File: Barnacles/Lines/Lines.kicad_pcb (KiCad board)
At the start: 2 copper layers, 10 x 88.8 mm, 6 parts

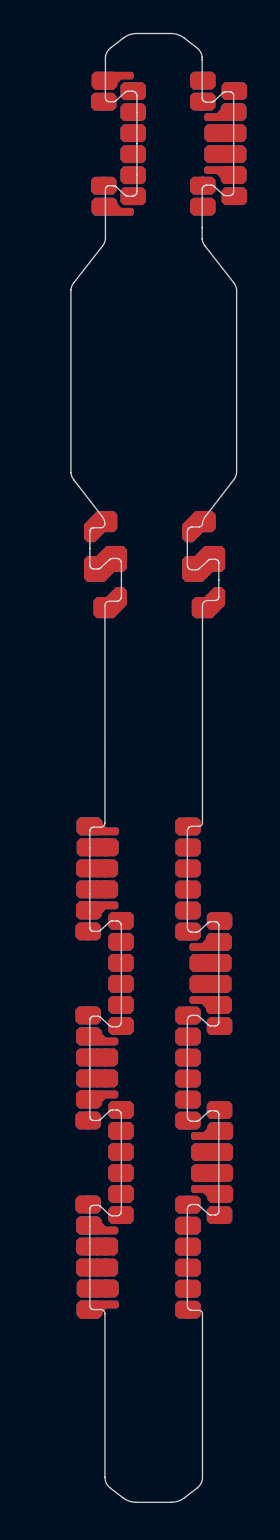
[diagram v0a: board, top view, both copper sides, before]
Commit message: actually route most of the barnacles
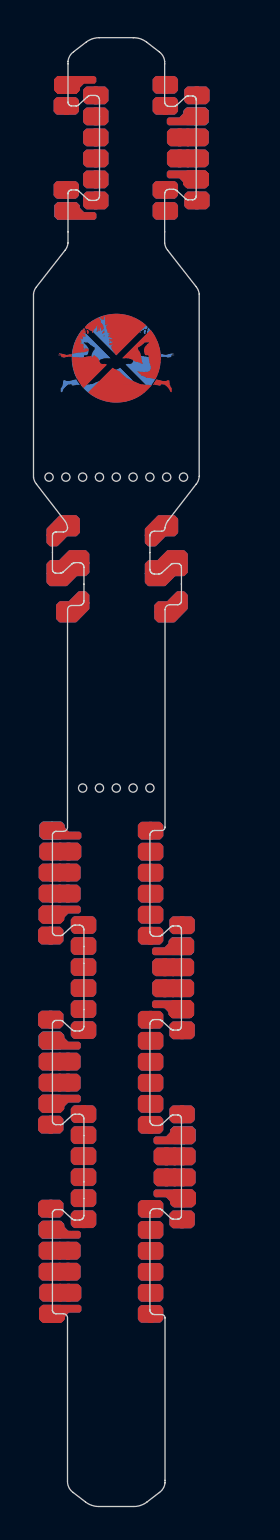
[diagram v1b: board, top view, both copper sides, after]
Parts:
- moved REF** 2.28 mm to (122.3, 84.9)
- moved REF** 2.28 mm to (116.5, 64.4)
- moved REF** 2.28 mm to (116.4, 84.7)
- moved REF** 2.28 mm to (122.3, 64.4)
- moved REF** 2.28 mm to (122.3, 130.1)
- moved REF** 2.28 mm to (116.4, 130.1)
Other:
- outline, holes or cut-outs redrawn
